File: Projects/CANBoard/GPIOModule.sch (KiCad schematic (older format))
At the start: 21 parts, among them J1_G1 HEADER_4, J2_G1 HEADER_4, J3_G1 HEADER_4, J4_G1 HEADER_4, J5_G1 HEADER_4, J5_G1 HEADER_6, J7_G1 HEADER_4, J8_G1 HEADER_4, U1_G1 74HC4051, U2_G1 74HC4051

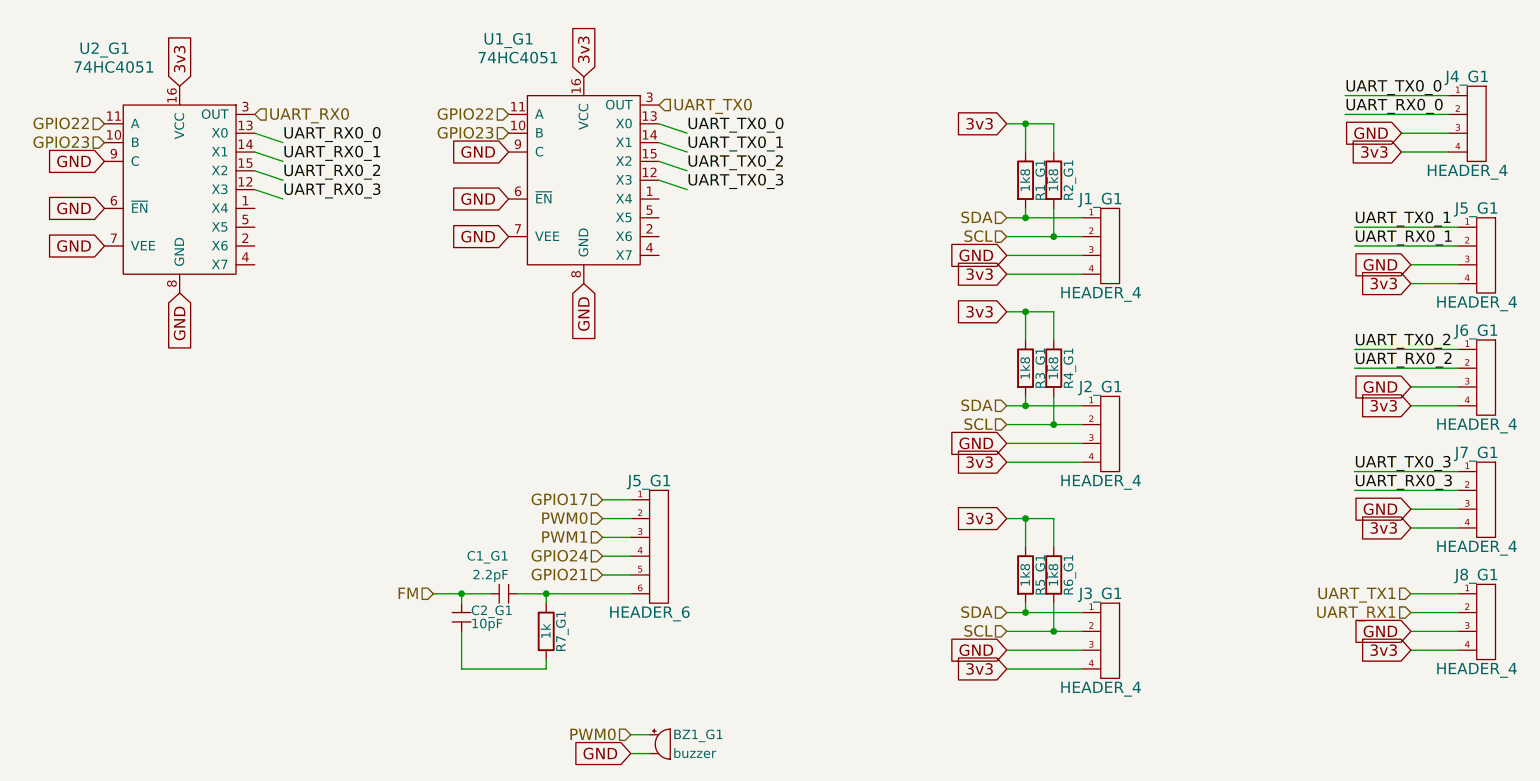
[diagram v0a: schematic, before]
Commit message: Major updates for power distribution and Communications boards
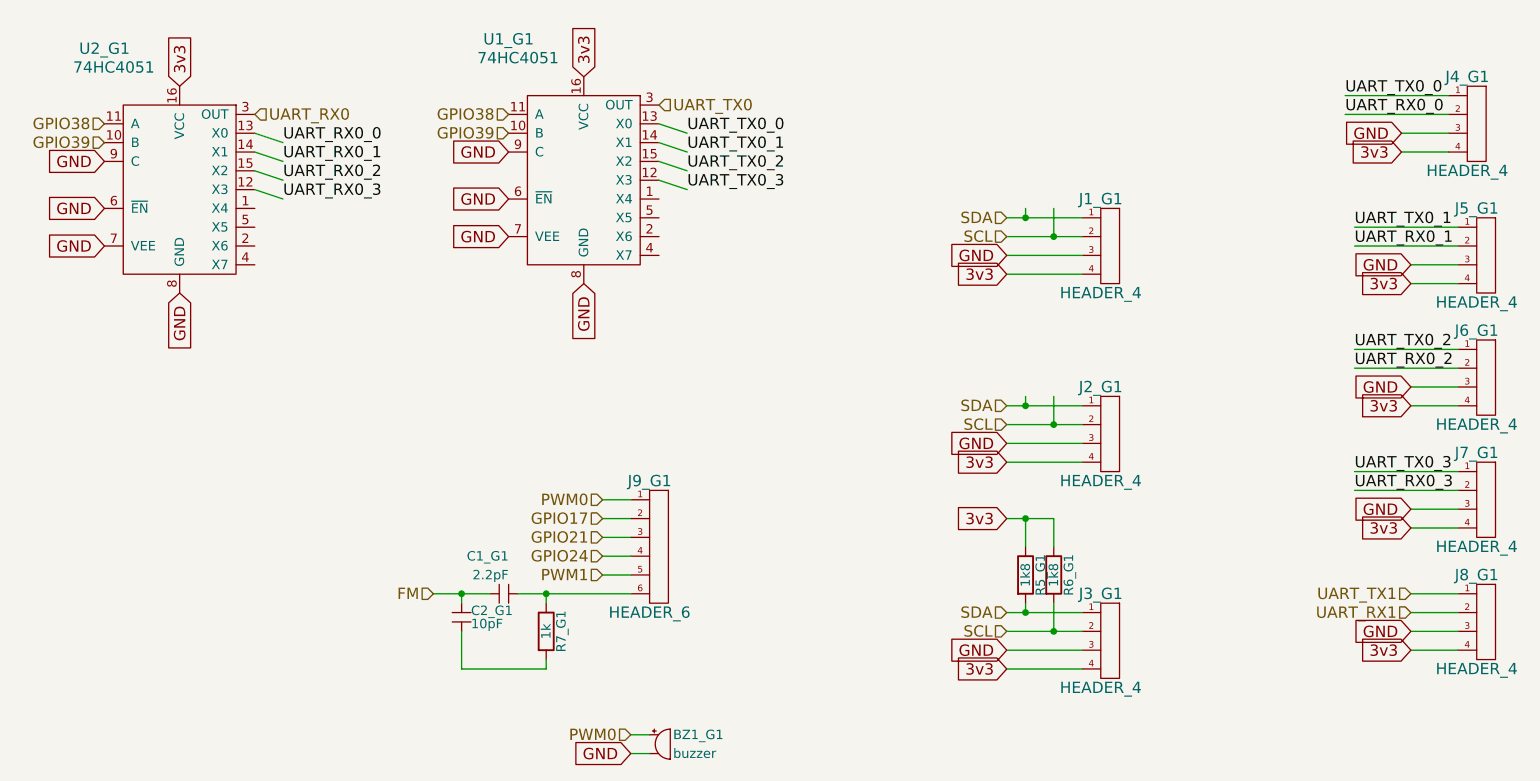
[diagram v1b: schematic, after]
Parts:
- removed R1_G1, R2_G1, R3_G1, R4_G1: 1k8, symbol R
- BZ1_G1: footprint (none) -> Buzzers_Beepers:MagneticBuzzer_Kingstate_KCG0601
- C1_G1, C2_G1: footprint (none) -> Capacitors_ThroughHole:C_Radial_D5_L11_P2.5
- J1_G1, J2_G1, J3_G1, J4_G1, J5_G1, J7_G1, J8_G1: footprint (none) -> Pin_Headers:Pin_Header_Straight_1x04
- J5_G1: footprint (none) -> Pin_Headers:Pin_Header_Straight_1x06
- R5_G1, R6_G1: footprint (none) -> Resistors_ThroughHole:Resistor_Horizontal_RM10mm
- U1_G1, U2_G1: footprint (none) -> Housings_DIP:DIP-16_W7.62mm
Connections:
- net labels added: GPIO38, GPIO39
- net labels removed: GPIO22, GPIO23
- wire segments 69 -> 63
